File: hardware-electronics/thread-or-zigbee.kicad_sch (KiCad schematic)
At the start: 2 parts, among them U5 CP2102N-A02-GQFN20, U7 EFR32MG21B020F1024IM32-B

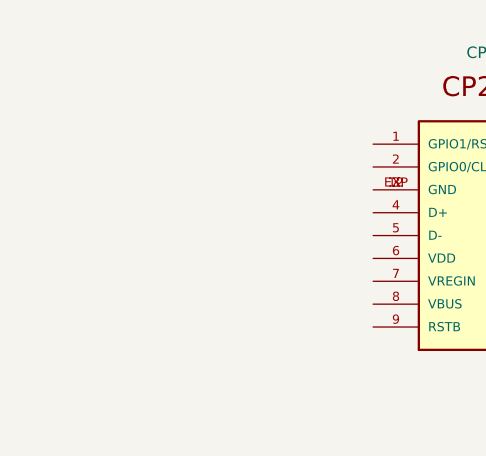
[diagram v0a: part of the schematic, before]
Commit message: SCH organise schematic #7
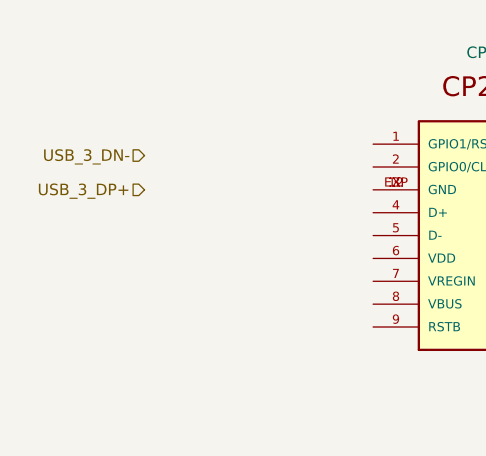
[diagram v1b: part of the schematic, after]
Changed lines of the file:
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@@
 	(generator_version "8.0")
 	(paper "A4")
+	(hierarchical_label "USB_3_DP+"
+		(shape input)
+		(at 90.17 60.96 180)
+		(fields_autoplaced yes)
+		(effects
+			(font
+				(size 1.27 1.27)
+			)
+			(justify right)
+		)
+	)
+	(hierarchical_label "USB_3_DN-"
+		(shape input)
+		(at 90.17 57.15 180)
+		(fields_autoplaced yes)
+		(effects
+			(font
+				(size 1.27 1.27)
+			)
+			(justify right)
+		)
+	)
 	(symbol
 		(lib_id "M2SmartHomeSymbols:EFR32MG21B020F1024IM32-B")

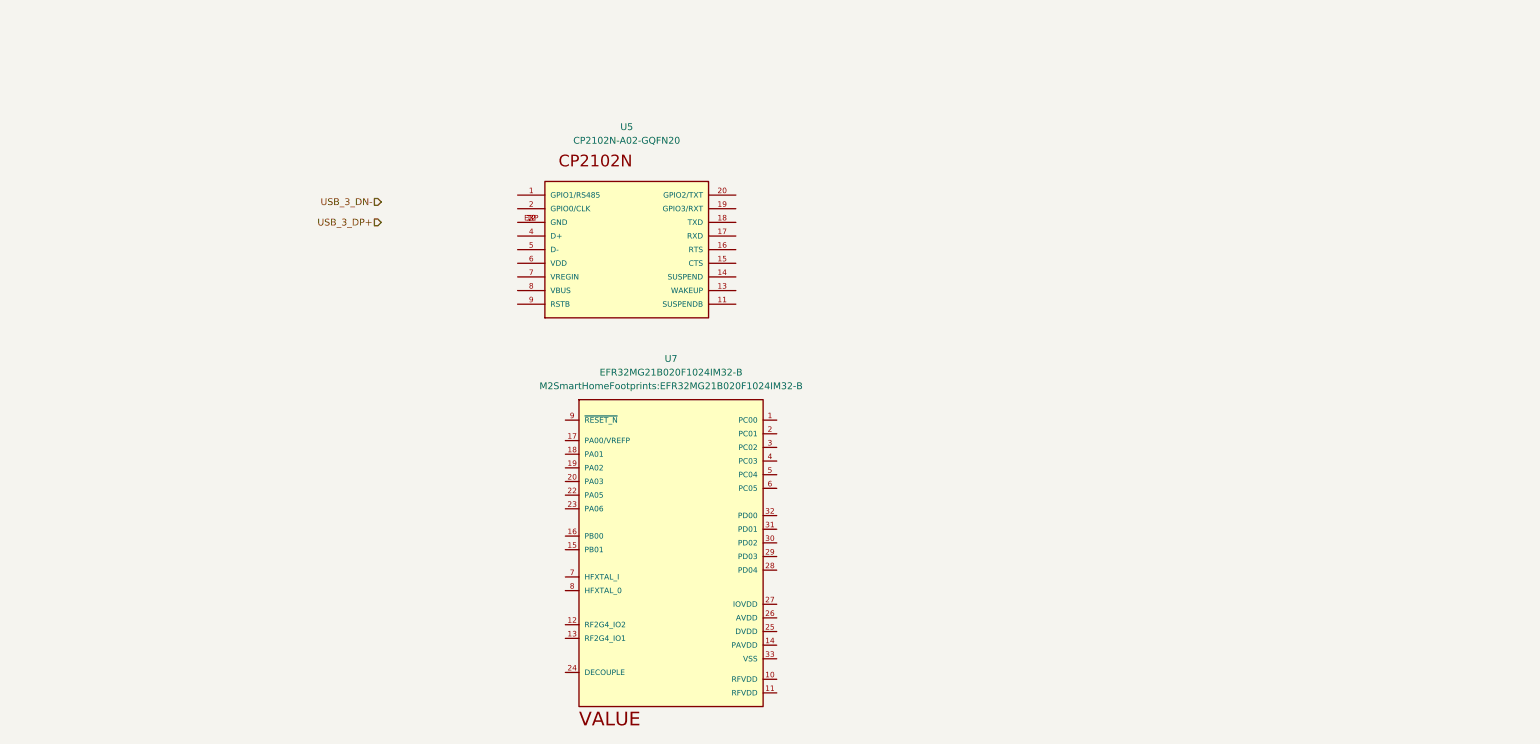
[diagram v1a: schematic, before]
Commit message: #12 WIP SCH thread/zigbee working on CP2102N connections
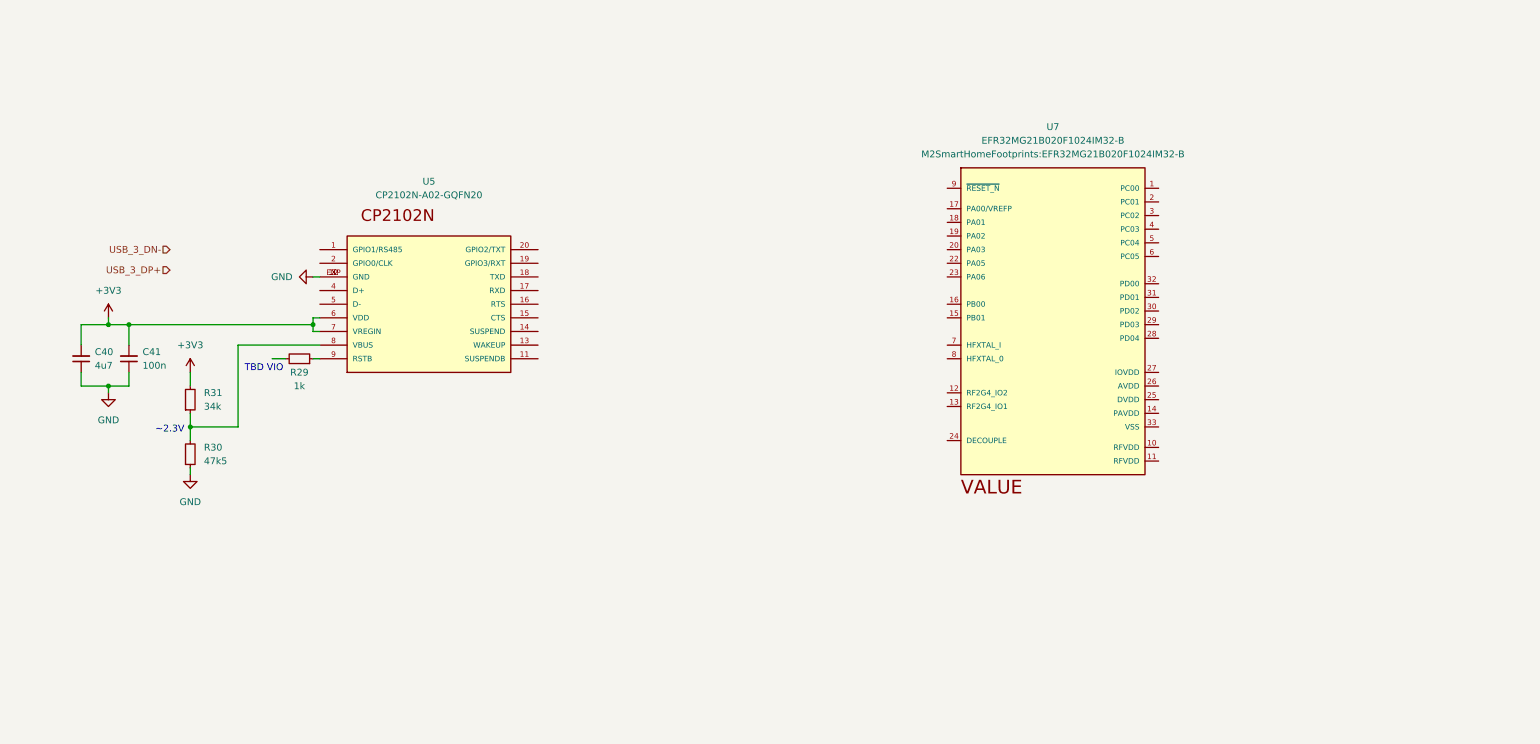
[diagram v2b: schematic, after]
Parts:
- added C40: C_4u7_0402, C_4u7_0402:C_0402_1005Metric, symbol M2SmartHomeSymbols:C_4u7_0402
- added C41: C_100n_0402, C_100n_0402:C_0402_1005Metric, symbol M2SmartHomeSymbols:C_100n_0402
- added R29: R_1k_0402, R_1k_0402:R_0402_1005Metric, symbol M2SmartHomeSymbols:R_1k_0402
- added R30: R_47k5_0402, R_47k5_0402:R_0402_1005Metric, symbol M2SmartHomeSymbols:R_47k5_0402
- added R31: R_34k_0402, R_34k_0402:R_0402_1005Metric, symbol M2SmartHomeSymbols:R_34k_0402
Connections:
- net GND: now reaches U5.12 (GND), U5.3 (GND), U5.EXP (GND)
- net GND: now also C40.1, C41.1, R30.1
- net +3V3: now reaches U5.6 (VDD)
- net +3V3: now also U5.7 (VREGIN), C40.2, C41.2, R31.2
- net at U5.8 (VBUS): now also R30.2, R31.1
- net at U5.9 (RSTB): now also R29.1
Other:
- note added: "TBD VIO"
- note added: "~2.3V"
- moved on the sheet: U5, U7

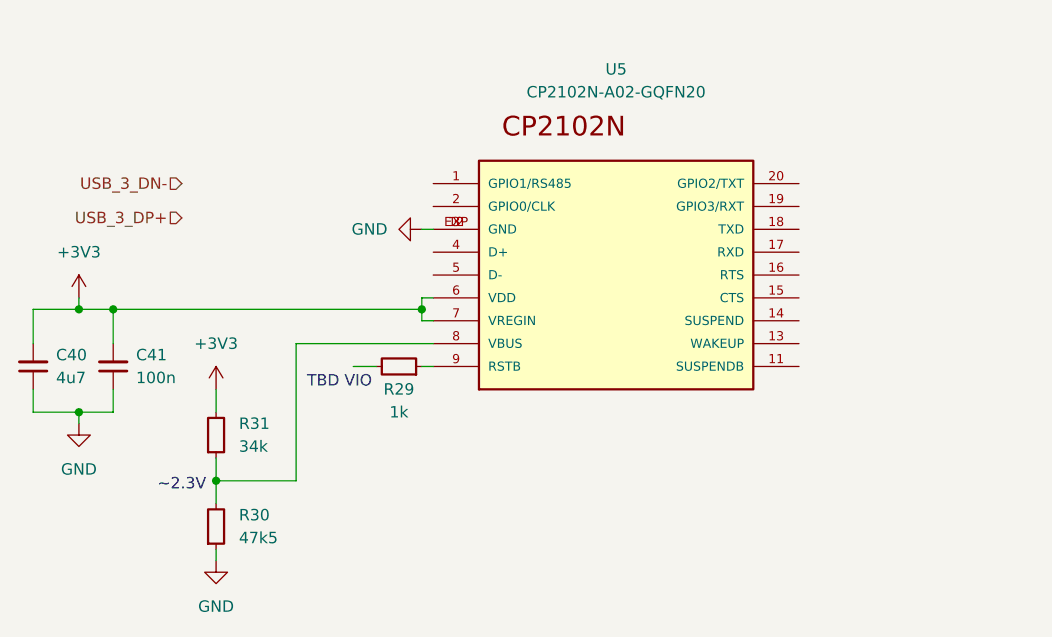
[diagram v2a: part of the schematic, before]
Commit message: #12 SCH thread/zigbee done CP2102N connections
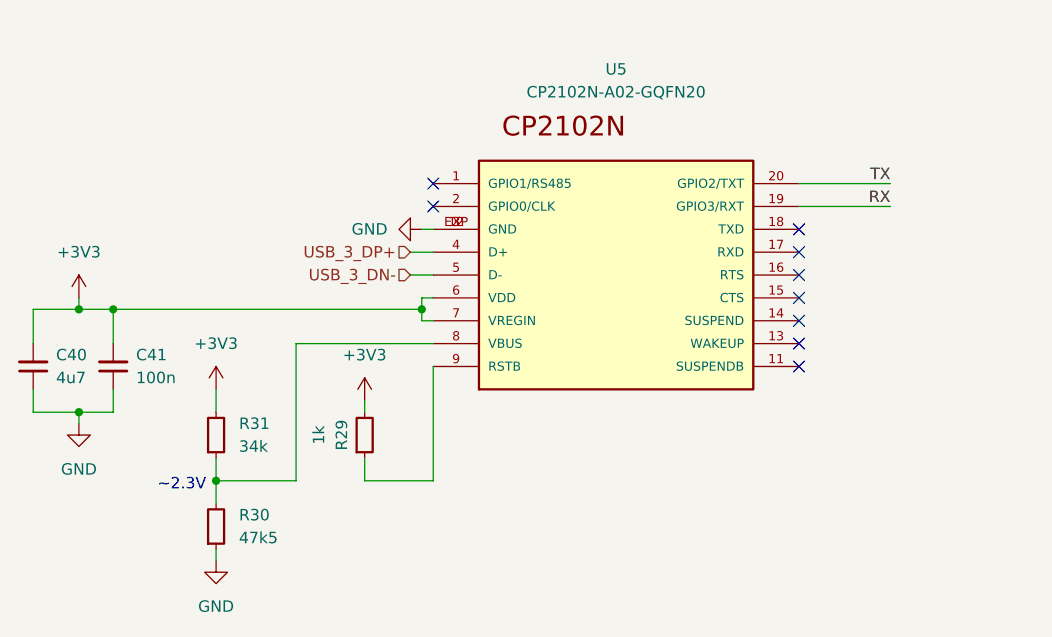
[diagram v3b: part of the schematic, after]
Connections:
- net +3V3: now also R29.2
- net USB_3_DN-: now also U5.5 (D-)
- net USB_3_DP+: now also U5.4 (D+)
- net RX: now reaches U5.19 (GPIO3/RXT)
- net TX: now reaches U5.20 (GPIO2/TXT)
- no-connect marks 0 -> 9
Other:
- note removed: "TBD VIO"
- moved on the sheet: R29
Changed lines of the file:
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@@
 		(color 0 0 0 0)
 	)
+	(no_connect
+		(at 119.38 78.74)
+	)
+	(no_connect
+		(at 119.38 81.28)
+	)
+	(no_connect
+		(at 119.38 86.36)
+	)
+	(no_connect
+		(at 119.38 76.2)
+	)
+	(no_connect
+		(at 119.38 83.82)
+	)
+	(no_connect
+		(at 78.74 68.58)
+	)
+	(no_connect
+		(at 78.74 66.04)
+	)
+	(no_connect
+		(at 119.38 71.12)
+	)
+	(no_connect
+		(at 119.38 73.66)
+	)
 	(wire
 		(pts
@@
 	(wire
 		(pts
+			(xy 71.12 99.06) (xy 78.74 99.06)
+		)
+		(stroke
+			(width 0)
+			(type default)
+		)
+	)
+	(wire
+		(pts
 			(xy 34.29 80.01) (xy 39.37 80.01)
 		)
@@
 	(wire
 		(pts
+			(xy 71.12 99.06) (xy 71.12 96.52)
+		)
+		(stroke
+			(width 0)
+			(type default)
+		)
+	)
+	(wire
+		(pts
 			(xy 77.47 81.28) (xy 78.74 81.28)
 		)
@@
 	(wire
 		(pts
+			(xy 71.12 90.17) (xy 71.12 91.44)
+		)
+		(stroke
+			(width 0)
+			(type default)
+		)
+	)
+	(wire
+		(pts
 			(xy 77.47 78.74) (xy 77.47 80.01)
 		)
@@
 	(wire
 		(pts
+			(xy 76.2 76.2) (xy 78.74 76.2)
+		)
+		(stroke
+			(width 0)
+			(type default)
+		)
+	)
+	(wire
+		(pts
 			(xy 54.61 99.06) (xy 54.61 101.6)
 		)
@@
 	(wire
 		(pts
-			(xy 77.47 86.36) (xy 78.74 86.36)
+			(xy 119.38 66.04) (xy 129.54 66.04)
 		)
 		(stroke
@@
 	(wire
 		(pts
+			(xy 78.74 99.06) (xy 78.74 86.36)
+		)
+		(stroke
+			(width 0)
+			(type default)
+		)
+	)
+	(wire
+		(pts
 			(xy 77.47 71.12) (xy 78.74 71.12)
 		)
@@
 	(wire
 		(pts
-			(xy 72.39 86.36) (xy 69.85 86.36)
+			(xy 76.2 73.66) (xy 78.74 73.66)
 		)
 		(stroke
@@
 		(pts
 			(xy 34.29 80.01) (xy 34.29 83.82)
+		)
+		(stroke
+			(width 0)
+			(type default)
+		)
+	)
+	(wire
+		(pts
+			(xy 119.38 68.58) (xy 129.54 68.58)
 		)
 		(stroke
@@
 		)
 	)
-	(text "TBD VIO"
-		(exclude_from_sim no)
-		(at 68.326 88.138 0)
-		(effects
-			(font
-				(size 1.27 1.27)
-			)
-		)
-	)
-	(hierarchical_label "USB_3_DP+"
-		(shape input)
-		(at 50.8 69.85 180)
+	(label "TX"
+		(at 129.54 66.04 180)
 		(fields_autoplaced yes)
 		(effects
@@
 				(size 1.27 1.27)
 			)
+			(justify right bottom)
+		)
+	)
+	(label "RX"
+		(at 129.54 68.58 180)
+		(fields_autoplaced yes)
+		(effects
+			(font
+				(size 1.27 1.27)
+			)
+			(justify right bottom)
+		)
+	)
+	(hierarchical_label "USB_3_DP+"
+		(shape input)
+		(at 76.2 73.66 180)
+		(fields_autoplaced yes)
+		(effects
+			(font
+				(size 1.27 1.27)
+			)
 			(justify right)
 		)
@@
 	(hierarchical_label "USB_3_DN-"
 		(shape input)
-		(at 50.8 66.04 180)
+		(at 76.2 76.2 180)
 		(fields_autoplaced yes)
 		(effects
@@
 	(symbol
 		(lib_id "M2SmartHomeSymbols:R_1k_0402")
-		(at 77.47 86.36 180)
+		(at 71.12 96.52 90)
 		(unit 1)
 		(exclude_from_sim no)
@@
 		(dnp no)
 		(property "Reference" "R29"
-			(at 74.93 88.9 0)
+			(at 68.58 93.98 0)
 			(effects
 				(font
@@
 		)
 		(property "Value" "R_1k_0402"
-			(at 57.15 73.66 0)
+			(at 83.82 76.2 0)
 			(effects
 				(font
@@
 		)
 		(property "Footprint" "R_1k_0402:R_0402_1005Metric"
-			(at 57.15 71.12 0)
+			(at 86.36 76.2 0)
 			(effects
 				(font
@@
 		)
 		(property "Datasheet" "https://www.vishay.com/docs/20035/crcw0402.pdf"
-			(at 57.15 68.58 0)
+			(at 88.9 76.2 0)
 			(effects
 				(font
@@
 		)
 		(property "Description" "SMD Thick Film Resistor, 1 kΩ, ±1%, 1/16 W, 0402 [1005 Metric], CRCW Series"
-			(at 77.47 86.36 0)
+			(at 71.12 96.52 0)
 			(effects
 				(font
@@
 		)
 		(property "MPN" "CRCW04021K00FKED"
-			(at 57.15 66.04 0)
+			(at 91.44 76.2 0)
 			(effects
 				(font
@@
 		)
 		(property "Manufacturer" "Vishay"
-			(at 57.15 63.5 0)
+			(at 93.98 76.2 0)
 			(effects
 				(font
@@
 		)
 		(property "License" "Apache-2.0"
-			(at 57.15 60.96 0)
+			(at 96.52 76.2 0)
 			(effects
 				(font
@@
 		)
 		(property "Author" "Your Name"
-			(at 57.15 58.42 0)
+			(at 99.06 76.2 0)
 			(effects
 				(font
@@
 		)
 		(property "Val" "1k"
-			(at 74.93 91.44 0)
+			(at 66.04 93.98 0)
 			(effects
 				(font
@@
 		)
 		(property "Tolerance" "1%"
-			(at 57.15 76.2 0)
+			(at 81.28 76.2 0)
 			(effects
 				(font
@@
 		)
 		(property "Power" "1/16 W"
-			(at 57.15 72.66 0)
+			(at 84.82 76.2 0)
 			(effects
 				(font
@@
 					(unit 1)
 				)
+			)
+		)
+	)
+	(symbol
+		(lib_id "power:+3V3")
+		(at 71.12 90.17 0)
+		(unit 1)
+		(exclude_from_sim no)
+		(in_bom yes)
+		(on_board yes)
+		(dnp no)
+		(fields_autoplaced yes)
+		(property "Reference" "#PWR0100"
+			(at 71.12 93.98 0)
+			(effects
+				(font
+					(size 1.27 1.27)
+				)
+				(hide yes)
+			)
+		)
+		(property "Value" "+3V3"
+			(at 71.12 85.09 0)
+			(effects
+				(font
+					(size 1.27 1.27)
+				)
+			)
+		)
+		(property "Footprint" ""
+			(at 71.12 90.17 0)
+			(effects
+				(font
+					(size 1.27 1.27)
+				)
+				(hide yes)
+			)
+		)
+		(property "Datasheet" ""
+			(at 71.12 90.17 0)
+			(effects
+				(font
+					(size 1.27 1.27)
+				)
+				(hide yes)
+			)
+		)
+		(property "Description" "Power symbol creates a global label with name \"+3V3\""
+			(at 71.12 90.17 0)
+			(effects
+				(font
+					(size 1.27 1.27)
+				)
+				(hide yes)
+			)
+		)
+		(pin "1"
+		)
+		(instances
+			(project "M2SmartHome"
+				(path "/da663dec-9e91-4003-a791-431d460ad63c/a351a459-aa5d-43cb-82d3-d5bdf9396bea"
+					(reference "#PWR0100")
+					(unit 1)
+				)

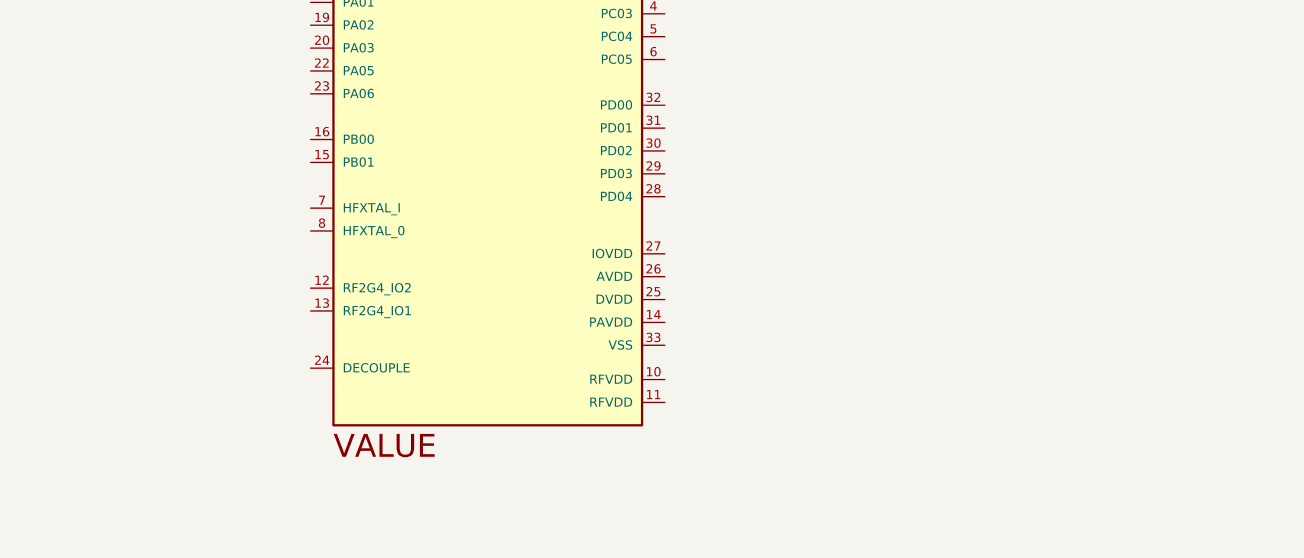
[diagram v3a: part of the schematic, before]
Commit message: #12 WIP SCH thread/zigbee working on EFR32MG21 connections
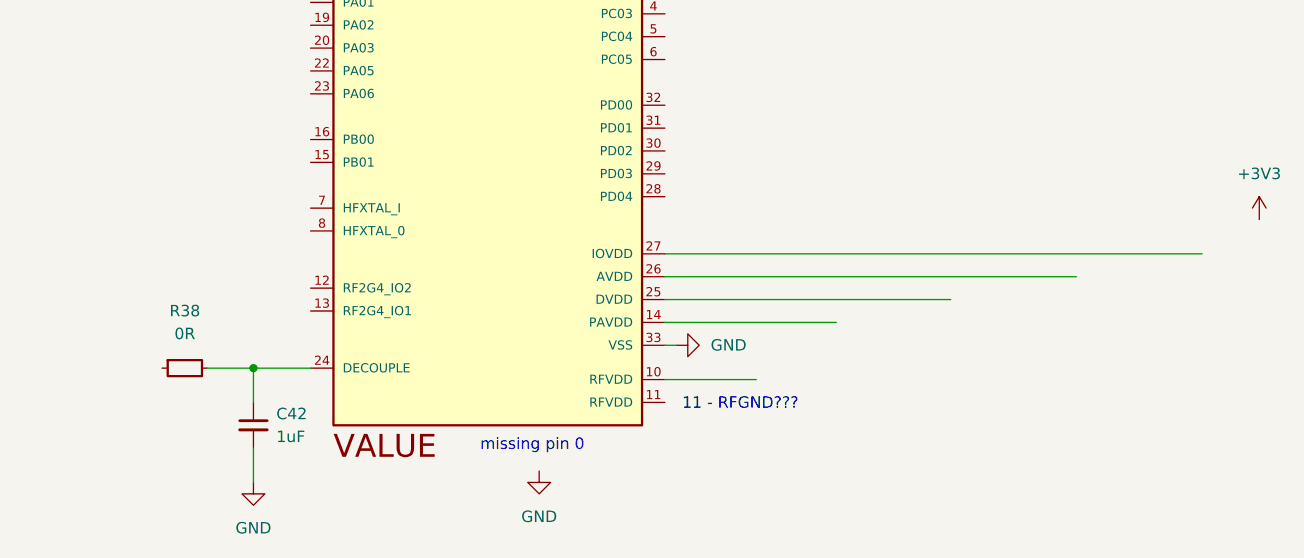
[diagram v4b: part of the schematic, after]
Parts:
- added C42: C_1uF_0402, C_1uF_0402:C_0402_1005Metric, symbol M2SmartHomeSymbols:C_1uF_0402
- added R38: R_0_0402, R_0_0402:R_0402_1005Metric, symbol M2SmartHomeSymbols:R_0_0402
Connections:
- net GND: now also U7.33 (VSS), C42.2
- net at U7.24 (DECOUPLE): now also C42.1, R38.2
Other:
- note added: "11 - RFGND???"
- note added: "missing pin 0"
